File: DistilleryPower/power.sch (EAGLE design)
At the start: 94 parts, among them IC1 ACS758LCB-050B-PFF-T, IC3 MICROCHIP_BY_ELEMENT14_BATCH_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, IC4 SN65HVD230/1, IC5 SN65HVD230/1, J1 GREEN-2P-5.0, J2 GREEN-2P-5.0, J3 GREEN-2P-5.0, J4 GREEN-2P-5.0, J5 GREEN-2P-5.0, Q1 BC807-16LT1SMD, T1 BT138-DSH, U1 STM32F042KXTX, U2 STM32F042KXTX, X1 IQD-FREQUENCY-PRODUCTS_CRYSTA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, X2 22-23-2041, X3 22-23-2041, X4 IQD-FREQUENCY-PRODUCTS_CRYSTA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

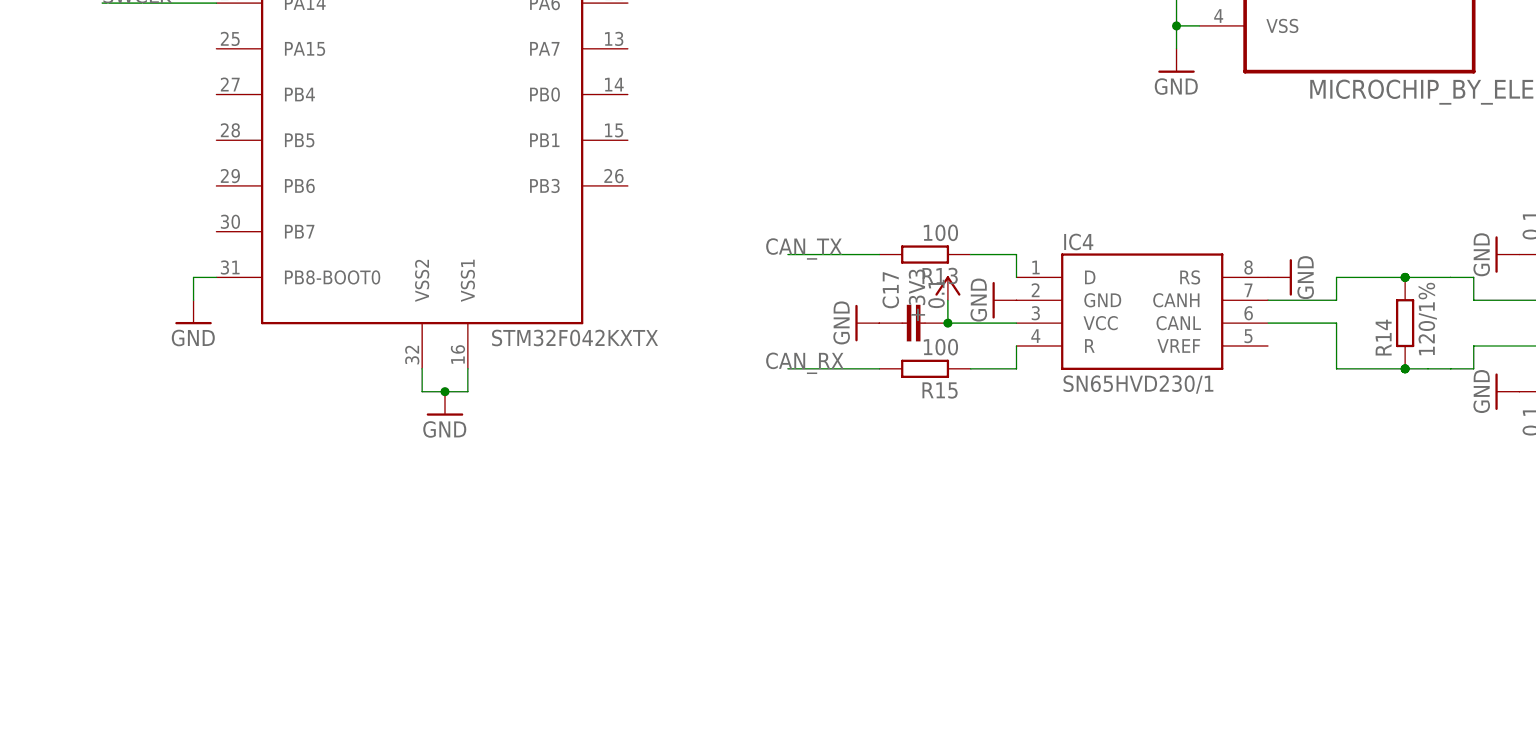
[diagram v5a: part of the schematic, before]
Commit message: added 1wire; finished profile layer
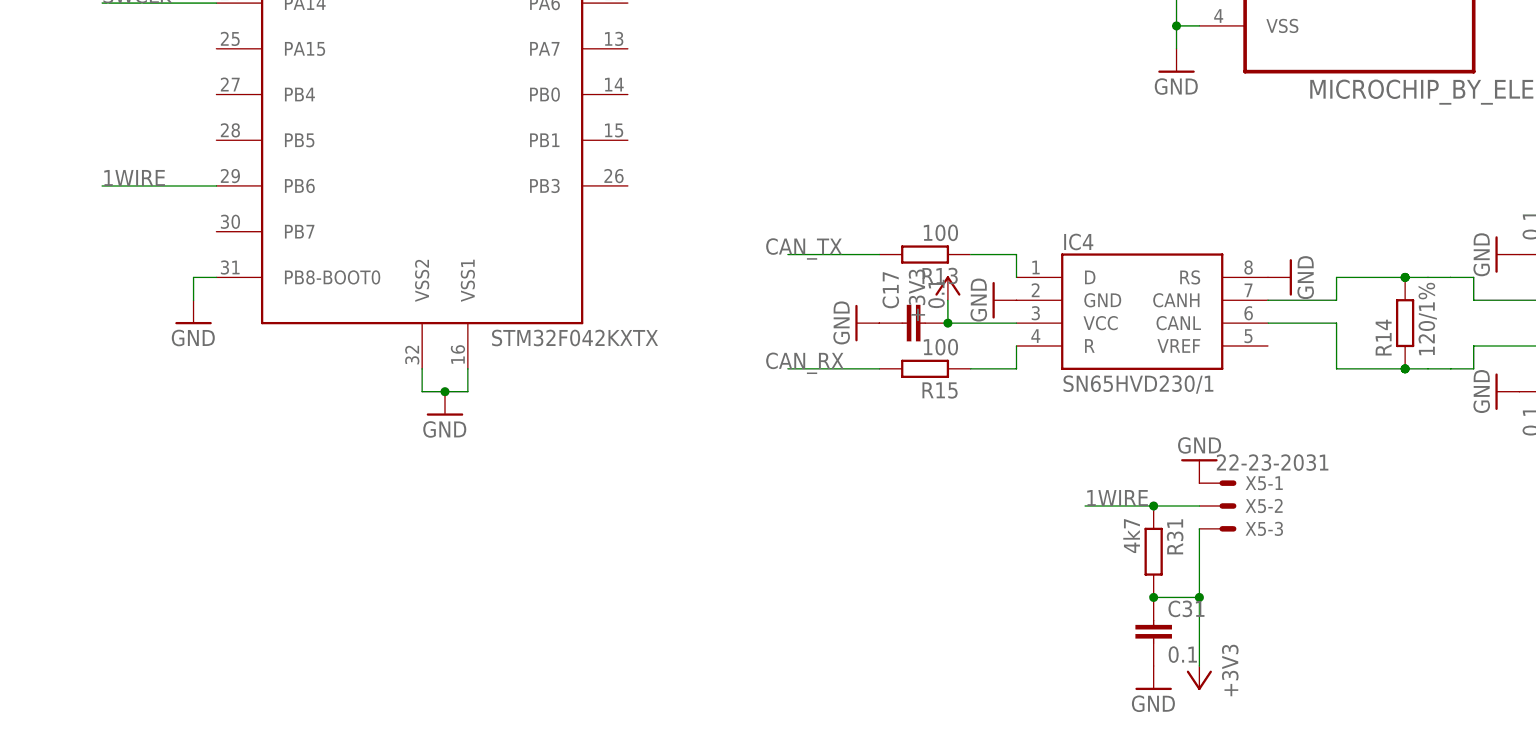
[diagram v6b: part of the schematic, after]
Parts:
- added C31: 0.1, rcl:C-EUC0603
- added R31: 4k7, rcl:R-EU_R0603
- added X5: 22-23-2031, con-molex:22-23-2031
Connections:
- new net 1WIRE: R31.1, U1.PB6, X5-2.S
- net +3V3: now also C31.1, R31.2, X5-3.S
- net GND: now also C31.2, X5-1.S
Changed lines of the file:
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@@
 <?xml version="1.0" encoding="utf-8"?>
 <!DOCTYPE eagle SYSTEM "eagle.dtd">
-<eagle version="9.1.0">
+<eagle version="9.1.3">
 <drawing>
 <settings>
@@
 <part name="GND37" library="supply1" deviceset="GND" device=""/>
 <part name="GND38" library="supply1" deviceset="GND" device=""/>
+<part name="X5" library="con-molex" library_urn="urn:adsk.eagle:library:165" deviceset="22-23-2031" device=""/>
+<part name="GND39" library="supply1" deviceset="GND" device=""/>
+<part name="+3V10" library="supply1" deviceset="+3V3" device=""/>
+<part name="R31" library="rcl" library_urn="urn:adsk.eagle:library:334" deviceset="R-EU_" device="R0603" package3d_urn="urn:adsk.eagle:package:23555/2" value="4k7"/>
+<part name="C31" library="rcl" deviceset="C-EU" device="C0603" value="0.1"/>
+<part name="GND40" library="supply1" deviceset="GND" device=""/>
 </parts>
 <sheets>
@@
 <instance part="GND37" gate="1" x="370.84" y="-104.14" rot="MR0"/>
 <instance part="GND38" gate="1" x="383.54" y="-104.14" rot="MR0"/>
+<instance part="X5" gate="-1" x="187.96" y="-116.84"/>
+<instance part="X5" gate="-2" x="187.96" y="-119.38"/>
+<instance part="X5" gate="-3" x="187.96" y="-121.92"/>
+<instance part="GND39" gate="1" x="185.42" y="-114.3" rot="R180"/>
+<instance part="+3V10" gate="G$1" x="185.42" y="-139.7" rot="R180"/>
+<instance part="R31" gate="G$1" x="180.34" y="-124.46" rot="R270"/>
+<instance part="C31" gate="G$1" x="180.34" y="-132.08"/>
+<instance part="GND40" gate="1" x="180.34" y="-139.7"/>
 </instances>
 <busses>
@@
 <pinref part="+3V310" gate="G$1" pin="+3V3"/>
 </segment>
+<segment>
+<pinref part="X5" gate="-3" pin="S"/>
+<pinref part="+3V10" gate="G$1" pin="+3V3"/>
+<wire x1="185.42" y1="-137.16" x2="185.42" y2="-129.54" width="0.1524" layer="91"/>
+<pinref part="R31" gate="G$1" pin="2"/>
+<wire x1="185.42" y1="-129.54" x2="185.42" y2="-121.92" width="0.1524" layer="91"/>
+<wire x1="180.34" y1="-129.54" x2="185.42" y2="-129.54" width="0.1524" layer="91"/>
+<junction x="185.42" y="-129.54"/>
+<pinref part="C31" gate="G$1" pin="1"/>
+<junction x="180.34" y="-129.54"/>
+</segment>
 </net>
 <net name="CUR_LOAD" class="0">
@@
 <pinref part="X2" gate="-1" pin="S"/>
 <pinref part="GND17" gate="1" pin="GND"/>
+</segment>
+<segment>
+<pinref part="X5" gate="-1" pin="S"/>
+<pinref part="GND39" gate="1" pin="GND"/>
+</segment>
+<segment>
+<pinref part="C31" gate="G$1" pin="2"/>
+<pinref part="GND40" gate="1" pin="GND"/>
 </segment>
 </net>
@@
 </segment>
 </net>
+<net name="1WIRE" class="0">
+<segment>
+<pinref part="U1" gate="G$1" pin="PB6"/>
+<wire x1="76.2" y1="-83.82" x2="63.5" y2="-83.82" width="0.1524" layer="91"/>
+<label x="63.5" y="-83.82" size="1.778" layer="95"/>
+</segment>
+<segment>
+<pinref part="X5" gate="-2" pin="S"/>
+<wire x1="185.42" y1="-119.38" x2="180.34" y2="-119.38" width="0.1524" layer="91"/>
+<label x="172.72" y="-119.38" size="1.778" layer="95"/>
+<pinref part="R31" gate="G$1" pin="1"/>
+<wire x1="180.34" y1="-119.38" x2="172.72" y2="-119.38" width="0.1524" layer="91"/>
+<junction x="180.34" y="-119.38"/>
+</segment>
+</net>
